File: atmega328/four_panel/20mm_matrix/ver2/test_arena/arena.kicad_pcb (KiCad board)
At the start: 2 copper layers, 260 x 50 mm, 41 parts, among them M1 VAL**, M2 VAL**, M3 VAL**, M4 VAL**, M5 VAL**, M6 VAL**, P1 CONN15, P10 CONN_2X2, P11 CONN_2X2, P12 CONN_2X2, P13 CONN_2X2, P14 CONN_2X2, P15 CONN_2X2, P16 CONN_2X2, P17 CONN_2X2, P18 CONN_2X2, P19 CONN_2X2, P2 CONN15, P20 CONN_2X2, P21 CONN_2X2, P22 CONN_20X2, P23 CONN_30X2, P24 CONN_2, P25 CONN_5X2, P26 CONN_5X2, P27 CONN_5X2, P28 CONN_5X2, P29 CONN_5X2, P3 CONN15, P30 CONN_20X2, P4 CONN15, P5 CONN15, P6 CONN15, P7 CONN_2X2, P8 CONN_2X2, P9 CONN_2X2

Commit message: Finished new test arena design - for atmega328 4x20mm panels v0.2
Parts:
- removed P10, P11, P12, P13, P14, P15, P16, P17, P18, P19, P20, P21: CONN_2X2, PIN_ARRAY_2X2
- removed P23: CONN_30X2, PIN_ARRAY_SHRD_30X2
- removed P24: CONN_2, DCJACK_2PIN
- removed P25, P26, P27, P28, P29: CONN_5X2, PIN_ARRAY_5x2
- removed P30: CONN_20X2, PIN_ARRAY_SHRD_20X2
- removed the P7 at (102.3, 66.0)
- added SW1: SWITCH_INV, slide_switch, F.Cu at (79.6, 94.9)
- P8: value CONN_2X2 -> CONN_34X2; footprint PIN_ARRAY_2X2 -> TE_CONN_DSUB_RA_68
- P9: value CONN_2X2 -> CONN_2; footprint PIN_ARRAY_2X2 -> DCJACK_2PIN_HIGHCURRENT
- moved P9 129.6 mm to (57.5, 100.0), turned to 180 degrees
- moved P8 99.6 mm to (236.1, 100.0)
- moved P7 17.6 mm to (127.6, 88.3)
- renumbered P22 to P7
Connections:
- C1 pad 1: +5V -> /VIN
- C2 pad 1: +5V -> /VIN
- C3 pad 1: +5V -> /VIN
- C4 pad 1: +5V -> /VIN
- C5 pad 1: +5V -> /VIN
- P1 pad 1: +5V -> /VIN
- P1 pad 10: /CS4_0 -> /CS3
- P1 pad 11: /CS5_0 -> /CS4
- P1 pad 12: /EXT_INT1 -> /CS5
- P1 pad 13: /RX -> /CS6
- P1 pad 14: /TX -> /CS7
- P1 pad 15: /EXT_INT0 -> /EXT_INT
- P1 pad 3: /RESET_MSTR -> /RESET
- P1 pad 7: /CS1_0 -> /CS0
- P1 pad 8: /CS2_0 -> /CS1
- P1 pad 9: /CS3_0 -> /CS2
- P2 pad 1: +5V -> /VIN
- P2 pad 10: /CS4_1 -> /CS3
- P2 pad 11: /CS5_1 -> /CS4
- P2 pad 12: /EXT_INT1 -> /CS5
- P2 pad 13: /RX -> /CS6
- P2 pad 14: /TX -> /CS7
- P2 pad 15: /EXT_INT0 -> /EXT_INT
- P2 pad 3: /RESET_MSTR -> /RESET
- P2 pad 4: /SCK_11 -> /SCK_1
- P2 pad 5: /MOSI_11 -> /MOSI_1
- P2 pad 6: /MISO_11 -> /MISO_1
- P2 pad 7: /CS1_1 -> /CS0
- P2 pad 8: /CS2_1 -> /CS1
- P2 pad 9: /CS3_1 -> /CS2
- P3 pad 1: +5V -> /VIN
- P3 pad 10: /CS4_2 -> /CS3
- P3 pad 11: /CS5_2 -> /CS4
- P3 pad 12: /EXT_INT1 -> /CS5
- P3 pad 13: /RX -> /CS6
- P3 pad 14: /TX -> /CS7
- P3 pad 15: /EXT_INT0 -> /EXT_INT
- P3 pad 3: /RESET_MSTR -> /RESET
- P3 pad 4: /SCK_22 -> /SCK_2
- P3 pad 5: /MOSI_22 -> /MOSI_2
- P3 pad 6: /MISO_22 -> /MISO_2
- P3 pad 7: /CS1_2 -> /CS0
- P3 pad 8: /CS2_2 -> /CS1
- P3 pad 9: /CS3_2 -> /CS2
- P4 pad 1: +5V -> /VIN
- P4 pad 10: /CS4_3 -> /CS3
- P4 pad 11: /CS5_3 -> /CS4
- P4 pad 12: /EXT_INT1 -> /CS5
- P4 pad 13: /RX -> /CS6
- P4 pad 14: /TX -> /CS7
- P4 pad 15: /EXT_INT0 -> /EXT_INT
- P4 pad 3: /RESET_MSTR -> /RESET
- P4 pad 4: /SCK_33 -> /SCK_3
- P4 pad 5: /MOSI_33 -> /MOSI_3
- P4 pad 6: /MISO_33 -> /MISO_3
- P4 pad 7: /CS1_3 -> /CS0
- P4 pad 8: /CS2_3 -> /CS1
- P4 pad 9: /CS3_3 -> /CS2
- P5 pad 1: +5V -> /VIN
- P5 pad 10: /CS4_4 -> /CS3
- P5 pad 11: /CS5_4 -> /CS4
- P5 pad 12: /EXT_INT1 -> /CS5
- P5 pad 13: /RX -> /CS6
- P5 pad 14: /TX -> /CS7
- P5 pad 15: /EXT_INT0 -> /EXT_INT
- P5 pad 3: /RESET_MSTR -> /RESET
- P5 pad 4: /SCK_44 -> /SCK_4
- P5 pad 5: /MOSI_44 -> /MOSI_4
- P5 pad 6: /MISO_44 -> /MISO_4
- P5 pad 7: /CS1_4 -> /CS0
- P5 pad 8: /CS2_4 -> /CS1
- P5 pad 9: /CS3_4 -> /CS2
- P6 pad 1: +5V -> /VIN
- P6 pad 10: /CS4_5 -> /CS3
- P6 pad 11: /CS5_5 -> /CS4
- P6 pad 12: /EXT_INT1 -> /CS5
- P6 pad 13: /RX -> /CS6
- P6 pad 14: /TX -> /CS7
- P6 pad 15: /EXT_INT0 -> /EXT_INT
- P6 pad 3: /RESET_MSTR -> /RESET
- P6 pad 4: /SCK_55 -> /SCK_5
- P6 pad 5: /MOSI_55 -> /MOSI_5
- P6 pad 6: /MISO_55 -> /MISO_5
- P6 pad 7: /CS1_5 -> /CS0
- P6 pad 8: /CS2_5 -> /CS1
- P6 pad 9: /CS3_5 -> /CS2
- P7 pad 1: /RESET_MSTR -> /SCK_0
- P7 pad 10: /CS2_3 -> /CS4
- P7 pad 11: /MISO_0 -> /SCK_5
- P7 pad 12: /CS3_3 -> /CS5
- P7 pad 13: /CS1_0 -> /MOSI_0
- P7 pad 14: /CS4_3 -> /CS6
- P7 pad 15: /CS2_0 -> /MISO_0
- P7 pad 16: /CS5_3 -> /CS7
- P7 pad 17: /CS3_0 -> /MOSI_1
- P7 pad 18: /CS1_4 -> N-0000058
- P7 pad 19: /CS4_0 -> /MISO_1
- P7 pad 2: /EXT_INT0 -> /CS0
- P7 pad 20: /CS2_4 -> N-0000059
- P7 pad 21: /CS5_0 -> /MOSI_2
- P7 pad 22: /CS3_4 -> N-0000060
- P7 pad 23: /CS1_1 -> /MISO_2
- P7 pad 24: /CS4_4 -> N-0000061
- P7 pad 25: /CS2_1 -> /MOSI_3
- P7 pad 26: /CS5_4 -> N-0000062
- P7 pad 27: /CS3_1 -> /MISO_3
- P7 pad 28: /CS1_5 -> N-0000063
- P7 pad 29: /CS4_1 -> /MOSI_4
- P7 pad 3: /RX -> /SCK_1
- P7 pad 30: /CS2_5 -> /EXT_INT
- P7 pad 31: /CS5_1 -> /MISO_4
- P7 pad 32: /CS3_5 -> N-0000064
- P7 pad 33: /CS1_2 -> /MOSI_5
- P7 pad 34: /CS4_5 -> /RESET
- P7 pad 35: /CS2_2 -> /MISO_5
- P7 pad 36: /CS5_5 -> N-0000065
- P7 pad 37: /CS3_2 -> N-0000066
- P7 pad 38: +5V -> /VIN
- P7 pad 39: /CS4_2 -> N-0000067
- P7 pad 4: /EXT_INT1 -> /CS1
- P7 pad 5: /TX -> /SCK_2
- P7 pad 6: /CS5_2 -> /CS2
- P7 pad 7: /SCK_0 -> /SCK_3
- P7 pad 8: /CS1_3 -> /CS3
- P7 pad 9: /MOSI_0 -> /SCK_4
- P8 pad 1: /SCK_0 -> GND
- P8 pad 2: /SCK_22 -> GND
- P8 pad 3: /SCK_2 -> GND
- P8 pad 4: /SCK_22 -> N-0000022
- P9 pad 1: /SCK_0 -> +5V
- P9 pad 2: /SCK_33 -> GND
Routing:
- net +5V: track 394.6 -> 19.2 mm, vias 1 -> 0
- net /TX: track 361.4 -> 0.00 mm
- net /CS6: track 0.00 -> 350.4 mm
- net /RX: track 340.8 -> 0.00 mm
- net /VIN: track 0.00 -> 335.1 mm
- net /RESET_MSTR: track 315.7 -> 0.00 mm, vias 2 -> 0
- net /EXT_INT0: track 313.6 -> 0.00 mm, vias 1 -> 0
- net /EXT_INT1: track 309.4 -> 0.00 mm, vias 2 -> 0
- net /CS4_0: track 308.4 -> 0.00 mm, vias 1 -> 0
- net /CS5_0: track 308.2 -> 0.00 mm, vias 3 -> 0
- net /CS3: track 0.00 -> 307.5 mm
- net /CS5: track 0.00 -> 307.4 mm, vias 0 -> 1
- net /CS7: track 0.00 -> 304.0 mm, vias 0 -> 1
- net /RESET: track 0.00 -> 302.7 mm
- net /CS2: track 0.00 -> 301.3 mm
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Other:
- net class Pwr: trace_width 1.016 -> 0.889
- board text added: "4x 20mm Atmega328 Test Arena v0.2 www.iorodeo.com"
- board text added: "NI SPI connector"
- board text added: "SPI Connector"
- board text removed: "0"
- board text removed: "1"
- board text removed: "2"
- board text removed: "3"
- board text removed: "4"
- board text removed: "4x 20mm Atmega328 Test Arena v0.1 www.iorodeo.com"
- board text removed: "5"
- board text removed: "CS-COMMON"
- board text removed: "MISO"
- board text removed: "MOSI"
- board text removed: "SCK"
- board text removed: "SPI 1X"
- board text removed: "SPI 1X, CS-COMMON"
- board text removed: "SPI 6X"

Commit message: Worked on v0.2 test arena for atmega328 4x20mm panels. Added mosfet switch for reset. Modified for chaining via the 20x2 header so that we can drive 12 columns of panels.
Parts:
- added P10: CONN_20X2, PIN_ARRAY_SHRD_20X2, F.Cu at (186.5, 87.5)
- added Q1: MOSFET_NCHAN, SOT23, F.Cu at (276.0, 71.3)
- added R1: 200, SM0805, F.Cu at (283.2, 74.3)
- added R2: 20k, SM0805, F.Cu at (276.7, 78.1)
- moved P8 18.5 mm to (254.6, 100.0)
- moved P7 3.35 mm to (124.3, 87.7)
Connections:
- P1 pad 3: /RESET -> /RESET_PAN
- P2 pad 3: /RESET -> /RESET_PAN
- P3 pad 3: /RESET -> /RESET_PAN
- P4 pad 3: /RESET -> /RESET_PAN
- P5 pad 3: /RESET -> /RESET_PAN
- P6 pad 3: /RESET -> /RESET_PAN
- P7 pad 38: /VIN -> N-0000080
- P8 pad 29: N-0000035 (its old number) -> /MOSI_7
- P8 pad 30: N-0000014 -> /MOSI_8
- P8 pad 31: N-0000017 -> /MOSI_9
- P8 pad 32: /EXT_INT -> /MOSI_10
- P8 pad 33: N-0000039 (its old number) -> /MOSI_11
- P8 pad 61: N-0000018 -> /MOSI_6
- P8 pad 62: N-0000036 (its old number) -> /MISO_6
- P8 pad 63: N-0000040 (its old number) -> /MISO_7
- P8 pad 64: N-0000043 -> /MISO_8
- P8 pad 65: N-0000046 -> /MISO_9
- P8 pad 66: N-0000027 (its old number) -> /MISO_10
- P8 pad 67: N-0000030 (its old number) -> /MISO_11
- P8 pad 68: N-0000033 -> /EXT_INT
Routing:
- net GND: track 381.0 -> 0.00 mm
- net /CS6: track 350.4 -> 0.00 mm
- net /VIN: track 335.1 -> 0.00 mm
- net /CS3: track 307.5 -> 0.00 mm
- net /CS5: track 307.4 -> 0.00 mm, vias 1 -> 0
- net /CS7: track 304.0 -> 0.00 mm, vias 1 -> 0
- net /RESET: track 302.7 -> 0.00 mm
- net /CS2: track 301.3 -> 0.00 mm
- net /CS1: track 299.1 -> 0.00 mm
- net /CS0: track 298.6 -> 0.00 mm
- net /CS4: track 296.9 -> 0.00 mm
- net /EXT_INT: track 283.8 -> 0.00 mm, vias 1 -> 0
- net /SCK_4: track 226.9 -> 0.00 mm, vias 1 -> 0
- net /MOSI_0: track 199.5 -> 0.00 mm
- net /MISO_0: track 192.4 -> 0.00 mm, vias 1 -> 0
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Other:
- board text added: "SPI 1"
- board text added: "SPI 2"
- board text removed: "SPI Connector"

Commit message: Modified pwr,gnd and reset_pan trace widths. Re-routed.
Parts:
- moved C1 12.1 mm to (77.6, 68.9)
- moved C2 12.1 mm to (118.6, 68.9)
- moved C3 12.1 mm to (158.6, 68.9)
- moved C4 12.1 mm to (199.6, 68.9)
- moved C5 12.1 mm to (238.6, 68.9)
- moved P8 4.91 mm to (259.5, 100.1)
- moved P7 2.35 mm to (122.0, 88.2)
- moved P10 2.35 mm to (184.2, 88.0)
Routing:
- net GND: track 0.00 -> 548.8 mm
- net /VIN: track 0.00 -> 371.1 mm, vias 0 -> 1
- net /CS5: track 0.00 -> 349.2 mm, vias 0 -> 1
- net /CS7: track 0.00 -> 349.0 mm, vias 0 -> 1
- net /CS4: track 0.00 -> 346.1 mm, vias 0 -> 3
- net /CS2: track 0.00 -> 346.0 mm, vias 0 -> 1
- net /CS1: track 0.00 -> 336.2 mm, vias 0 -> 2
- net /EXT_INT: track 0.00 -> 334.5 mm, vias 0 -> 2
- net /CS6: track 0.00 -> 327.6 mm, vias 0 -> 4
- net /CS3: track 0.00 -> 326.2 mm, vias 0 -> 4
- net /CS0: track 0.00 -> 322.5 mm, vias 0 -> 2
- net /RESET_PAN: track 0.00 -> 278.8 mm, vias 0 -> 1
- net /MISO_3: track 0.00 -> 227.1 mm, vias 0 -> 1
- net /MOSI_0: track 0.00 -> 218.8 mm
- net /MISO_4: track 0.00 -> 217.5 mm, vias 0 -> 1
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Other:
- net class Pwr: trace_width 0.889 -> 0.635
- net class Reset_Pan added: clearance 0.254, trace_width 0.635, via_dia 0.889, via_drill 0.635
- board text added: "SPI 20x2 #1"
- board text added: "SPI 20x2 #2"
- board text removed: "SPI 1"
- board text removed: "SPI 2"

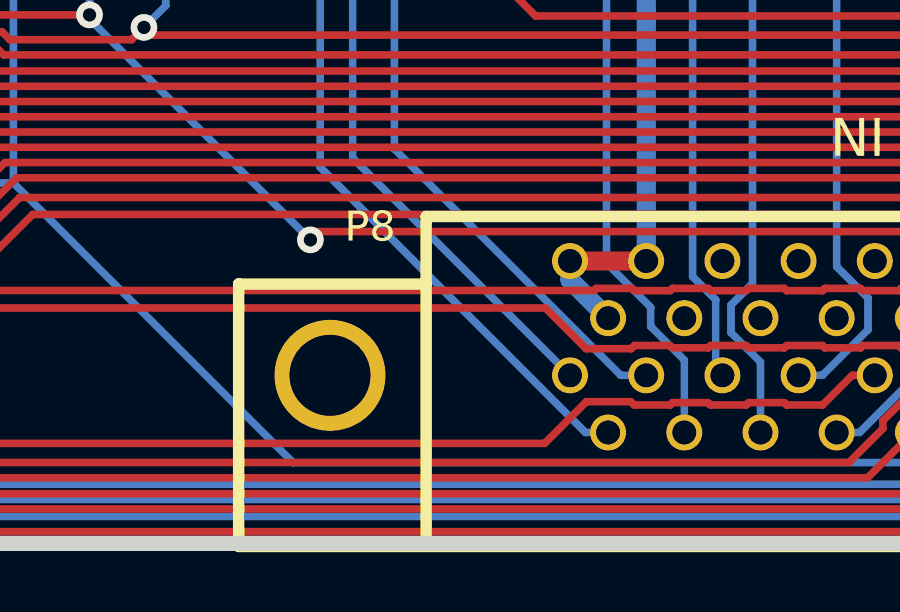
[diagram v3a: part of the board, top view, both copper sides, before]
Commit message: Added gerber files for new arena design.
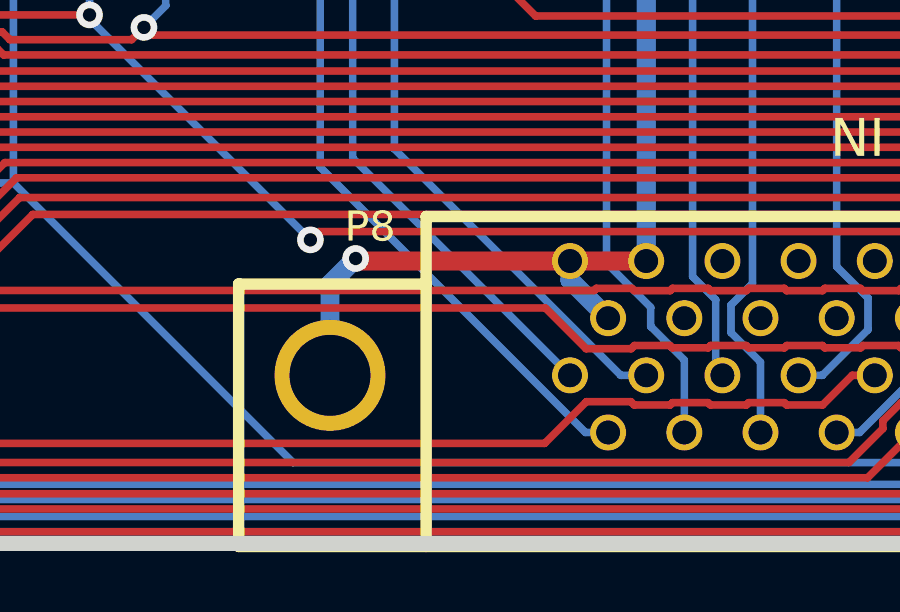
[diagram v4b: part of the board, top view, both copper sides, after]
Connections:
- P8 pad 69: (no net) -> GND
- P8 pad 70: (no net) -> N-0000067
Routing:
- net GND: track 548.8 -> 560.2 mm, vias 0 -> 1
